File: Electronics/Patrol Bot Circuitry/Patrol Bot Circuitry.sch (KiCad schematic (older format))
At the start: 2 parts

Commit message: A lot
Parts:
- added J?: Conn_01x08, symbol Connector_Generic:Conn_01x08
- added U?: TB6612FNG, Package_SO:SSOP-24_5.3x8.2mm_P0.65mm, symbol Driver_Motor:TB6612FNG
- added U?: MP1584EN, symbol MP1584EN:MP1584EN
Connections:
- net labels added: 3.3V
- wire segments 2 -> 31
- no-connect marks 0 -> 4
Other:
- note added: "ESP-32 Cam\n"
- note added: "Must have pin headers for ESP \nb/c it must be removed when \nuploading since IO0, IO3, and \nIO1 must be used during \nflashing. However, during \nruntime, those pins can be \nused as outputs."
- moved on the sheet: U?

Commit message: Update
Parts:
- removed J?: Conn_01x08, symbol Connector_Generic:Conn_01x08
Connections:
- no-connect marks 4 -> 10
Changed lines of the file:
@@
 $EndComp
-Wire Wire Line
-	4350 5800 4600 5800
-Wire Wire Line
-	4600 5800 4600 4250
-Wire Wire Line
-	4600 4250 4650 4250
-Wire Wire Line
-	4350 5700 4550 5700
-Wire Wire Line
-	4550 5700 4550 4150
-Wire Wire Line
-	4550 4150 4650 4150
-Wire Wire Line
-	4350 5500 4500 5500
-Wire Wire Line
-	4500 5500 4500 4050
-Wire Wire Line
-	4500 4050 4650 4050
-Wire Wire Line
-	4350 5400 4450 5400
-Wire Wire Line
-	4450 5400 4450 3950
-Wire Wire Line
-	4450 3950 4650 3950
 Wire Wire Line
 	4350 5300 4400 5300
@@
 	-1   0    0    1
 $EndComp
-$Comp
-L Connector_Generic:Conn_01x08 J?
-U 1 1 61A3F5ED
-P 2350 3850
-F 0 "J?" H 2430 3842 50  0000 L CNN
-F 1 "Conn_01x08" H 2430 3751 50  0000 L CNN
-F 2 "" H 2350 3850 50  0001 C CNN
-F 3 "~" H 2350 3850 50  0001 C CNN
-	1    2350 3850
-	1    0    0    -1
-$EndComp
+NoConn ~ 3450 6600
+NoConn ~ 3550 6600
+NoConn ~ 3650 6600
+NoConn ~ 3650 4600
+NoConn ~ 3450 4600
+NoConn ~ 5850 3550
+Wire Wire Line
+	4450 5400 4450 3950
+Wire Wire Line
+	4450 3950 4650 3950
+Wire Wire Line
+	4350 5400 4450 5400
+Wire Wire Line
+	4350 5500 4500 5500
+Wire Wire Line
+	4500 5500 4500 4050
+Wire Wire Line
+	4500 4050 4650 4050
+Wire Wire Line
+	4350 5700 4550 5700
+Wire Wire Line
+	4550 5700 4550 4150
+Wire Wire Line
+	4550 4150 4650 4150
+Wire Wire Line
+	4350 5800 4600 5800
+Wire Wire Line
+	4600 5800 4600 4250
+Wire Wire Line
+	4600 4250 4650 4250
 $EndSCHEMATC

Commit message: Update
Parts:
- added D?: D_Photo, symbol Device:D_Photo
- added R?: R, symbol Device:R
- added U?: MCP23017-E_SP, DIP787W45P254L3556H508Q28, symbol MCP23017-E_SP:MCP23017-E_SP
- added U?: MAX9814, symbol MAX9814_:MAX9814
- added U? (x2): HC-SR04, XCVR_HC-SR04, symbol HC-SR04:HC-SR04
- added U?: ADS1115, symbol ADS1115:ADS1115
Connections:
- net 3.3V: now also D?.2 (A)
- net GND: now also R?.2, U?.10 (VSS), U?.15 (A0), U?.16 (A1), U?.17 (A2), U?.2 (GND), U?.4 (GND), U?.4 (GND), U?.5 (ADDR), U?.5 (GND)
- net at U?.4 (OUTPUT-): now also U?.P$2 (GND); no longer U?.P$1 (5V)
- net SDA: now reaches U?.P$10 (IO1/U0T)
- net SDA: now also U?.13 (SDA), U?.4 (SDA)
- net SCL: now reaches U?.P$11 (IO3/U0R)
- net SCL: now also U?.12 (SCL), U?.3 (SCL)
- net 5V: now reaches U?.1 (OUTPUT+)
- net 5V: now also U?.P$1 (5V), U?.1 (VCC), U?.1 (VCC), U?.1 (VDD), U?.4 (VCC), U?.9 (VDD); no longer U?.P$2 (GND)
- new net: U?.1 (GPB0), U?.2 (TRIG)
- new net: U?.2 (GPB1), U?.3 (ECHO)
- new net: U?.2 (TRIG), U?.7 (GPB6)
- new net: U?.3 (ECHO), U?.8 (GPB7)
- new net: D?.1 (K), R?.1, U?.8 (A1)
- new net A0: U?.2 (OUT), U?.7 (A0)
- no-connect marks 10 -> 11
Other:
- note added: "1"
- note added: "11/27/2021\n"
- note added: "Connect ADDR to \nGND for address 0x48,\nVDD for address 0x49,\nSDA for address 0x4A,\nSCL for address 0x4B"
- moved on the sheet: U?

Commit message: Circuit Update
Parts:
- removed U?: TB6612FNG, Package_SO:SSOP-24_5.3x8.2mm_P0.65mm, symbol Driver_Motor:TB6612FNG
- added J?: Conn_01x03_Male, symbol Connector:Conn_01x03_Male
- added J? (x2): Screw_Terminal_01x02, symbol Connector:Screw_Terminal_01x02
- added J?: Left_Motor, symbol Connector:Screw_Terminal_01x02
- added J?: Right_Motor, symbol Connector:Screw_Terminal_01x02
- added Q? (x2): IRF4905, Package_TO_SOT_THT:TO-220-3_Vertical, symbol Transistor_FET:IRF4905
- added Q?: IRLZ44N, Package_TO_SOT_THT:TO-220-3_Vertical, symbol Transistor_FET:IRLZ44N
- added R?: 600K, symbol Device:R
- added R?: 200K, symbol Device:R
- added R?: 2K, symbol Device:R
- added U?: ROB-14450, MODULE_ROB-14450, symbol ROB-14450:ROB-14450
- added VR?: LM317T_NOPB, TO254P1054X470X1955-3, symbol LM317T_NOPB:LM317T_NOPB
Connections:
- net 3.3V: now also U?.4 (VCC)
- net 5V: now also J?.2 (Pin_2), Q?.2 (D), Q?.3 (S), U?.2 (VCC); no longer U?.1 (OUTPUT+), U?.4 (VCC)
- net GND: now also U?.10 (A3), U?.3 (OUTPUT-), U?.4 (OUTPUT-), U?.6 (INPUT-), U?.P$2 (GND), J?.1 (Pin_1), J?.1 (Pin_1), J?.1 (Pin_1), R?.2, U?.3 (GND)
- net SCL: now also U?.23 (SCL), U?.P$15 (IO16); no longer U?.P$11 (IO3/U0R)
- net SDA: now also U?.24 (SDA), U?.P$14 (IO0); no longer U?.P$10 (IO1/U0T)
- net at U?.P$3 (IO12): now also U?.16 (PWMA)
- net at U?.P$4 (IO13): now also U?.15 (AI1)
- net at U?.P$5 (IO15): now also U?.14 (AI2)
- net at U?.P$6 (IO14): now also U?.12 (BI1)
- net at U?.P$7 (IO2): now also U?.11 (BI2)
- net at U?.P$8 (IO4): now also U?.10 (PWMB)
- net 10VOut: now reaches U?.2 (OUTPUT+)
- net 10VOut: now also Q?.3 (S)
- net +10V: now reaches U?.7 (INPUT+)
- net +10V: now also J?.2 (Pin_2), VR?.3 (VIN)
- net at D?.1 (K), R?.1: now also U?.9 (A2); no longer U?.8 (A1)
- net VCC: no longer names the net of U?.8 (INPUT+)
- net VCC: now also Q?.3 (S)
- new net: R?.2, VR?.1 (ADJ)
- new net: J?.1 (Pin_1), U?.4 (A01)
- new net: J?.2 (Pin_2), U?.5 (A02)
- new net: J?.1 (Pin_1), U?.6 (B01)
- new net: J?.2 (Pin_2), U?.7 (B02)
- new net 10V: Q?.1 (G), Q?.1 (G), Q?.1 (G), U?.1 (VM)
- new net A1: R?.1, R?.2, U?.8 (A1)
- new net Battery: J?.2 (Pin_2), Q?.2 (D), R?.1, R?.1, VR?.2 (VOUT)
- new net BatteryOut: Q?.2 (D), U?.1 (OUTPUT+)
- new net IO3: J?.3 (Pin_3), U?.P$11 (IO3/U0R)
- no-connect marks 11 -> 36
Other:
- note added: "ADC for converting sensor readings\nto digital signals for monitoring."
- note added: "Accelerometer and gyroscope sensor."
- note added: "Buck converter that steps down\n10V to 5V for the esp32-cam."
- note added: "Charges the battery when connected\nto electrical outlet. ~~0.67 mA\n"
- note added: "H-Bridge that allows \nsignal amplification for\ncontrolling DC motor."
- note added: "Microphone for picking up sounds\nand detecting danger."
- note added: "Provide addition GPIO pins."
- note added: "Screw terminal for power supplies."
- note added: "See below for reference to ESP32 with servo:\nhttps://randomnerdtutorials.com/esp32-cam-pan-and-tilt-2-axis/"
- note added: "Sonar sensors for providing physical space\ndetection and room memory."
- note added: "Switch circuit that switches to 10V\ninput power supply when it is present \nand charges battery."
- note added: "Voltage divider to monitor battery voltage.\n"
- moved on the sheet: D?, R?, U?

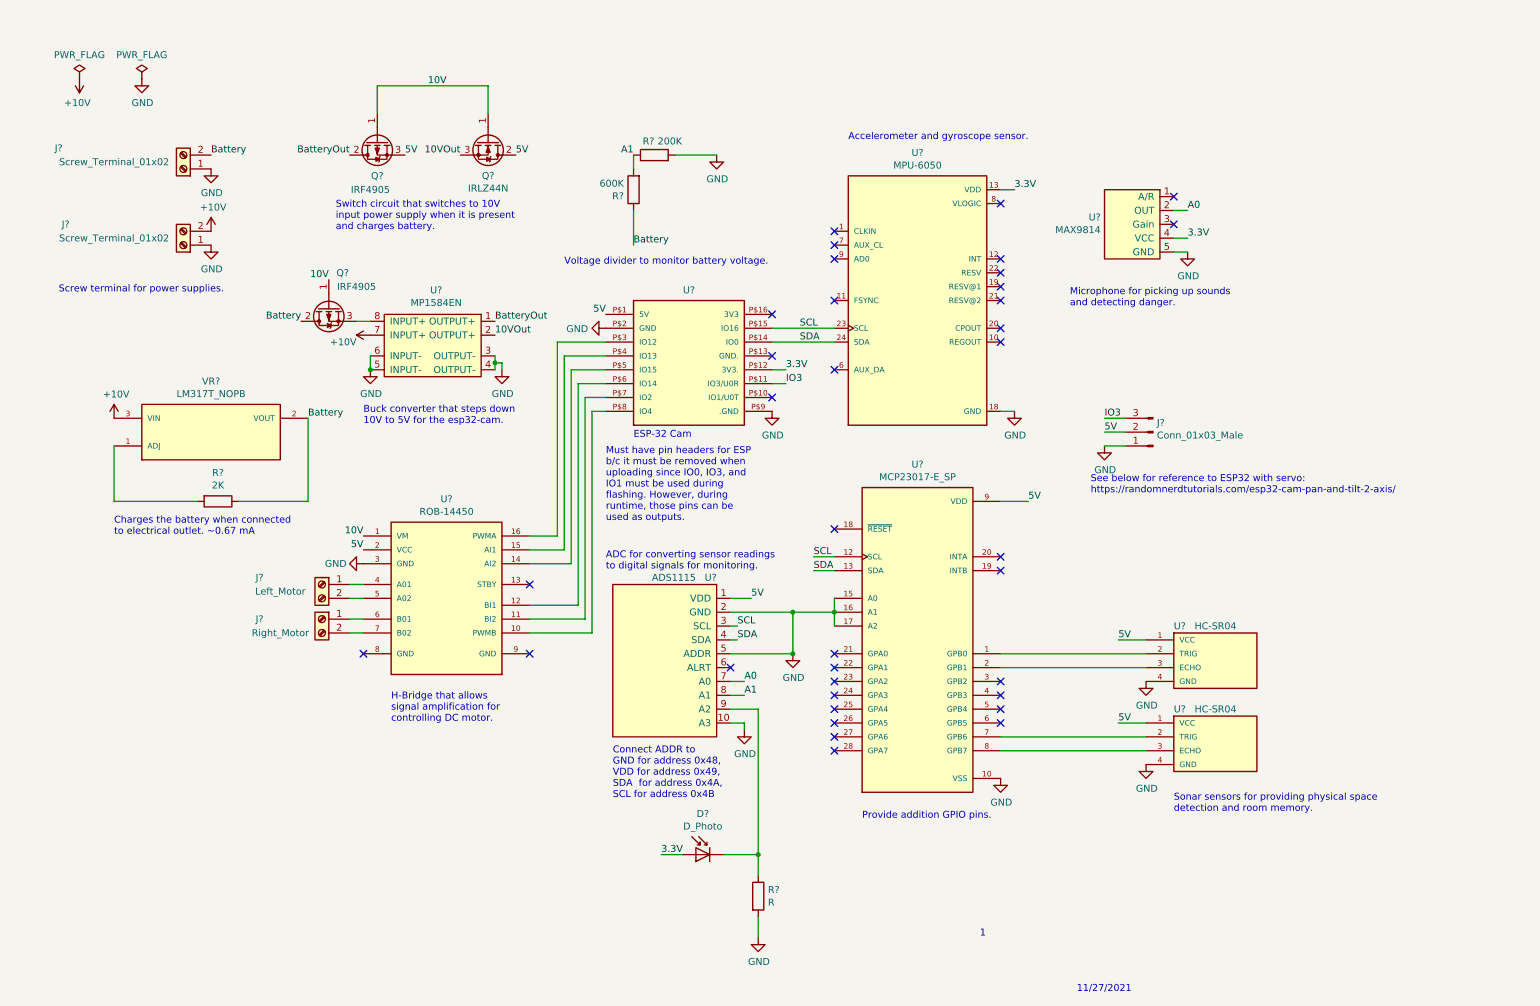
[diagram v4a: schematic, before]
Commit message: Reorganized schematic to aid debugging.
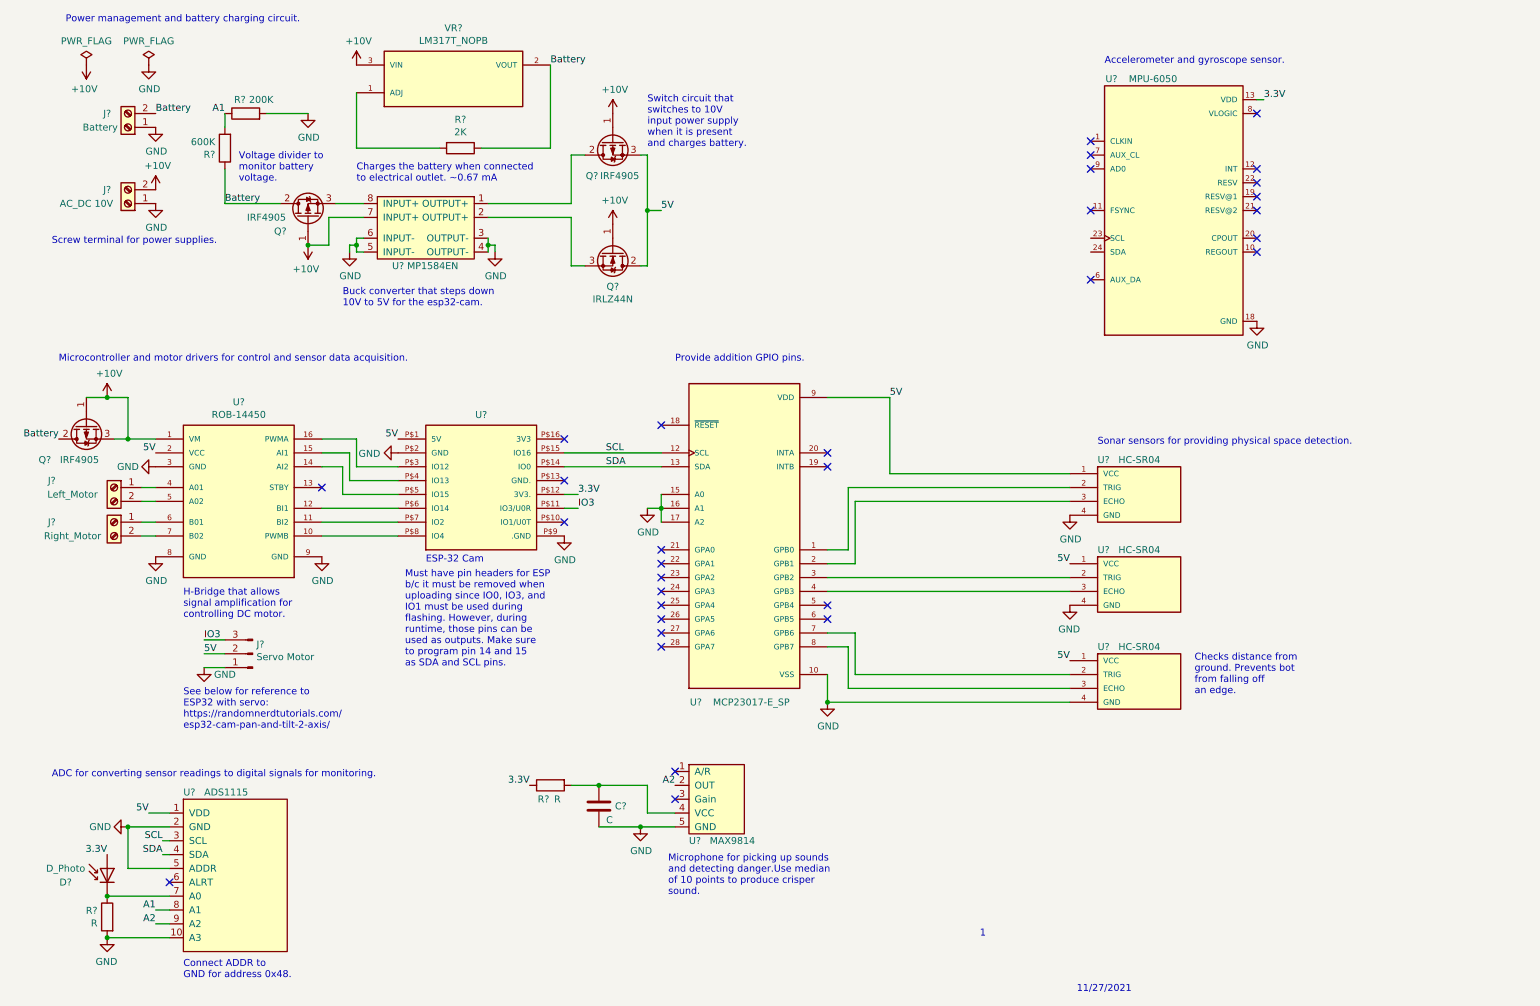
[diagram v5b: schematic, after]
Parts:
- added C?: C, symbol Device:C
- added Q?: IRF4905, Package_TO_SOT_THT:TO-220-3_Vertical, symbol Transistor_FET:IRF4905
- added R?: R, symbol Device:R
- added U?: HC-SR04, XCVR_HC-SR04, symbol HC-SR04:HC-SR04
- J?: value Conn_01x03_Male -> Servo Motor
- J?: value Screw_Terminal_01x02 -> Battery
- J?: value Screw_Terminal_01x02 -> AC_DC 10V
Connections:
- net 10V is gone; now on net +10V: Q?.1 (G), Q?.1 (G), Q?.1 (G), U?.1 (VM)
- net +10V: now also Q?.1 (G), Q?.3 (S)
- net 3.3V: now also R?.1; no longer U?.4 (VCC)
- net 5V: now also U?.1 (VCC)
- net Battery: now also Q?.2 (D)
- net GND: now also U?.8 (GND), U?.9 (GND), C?.2, U?.4 (GND)
- net SCL: no longer U?.23 (SCL)
- net SDA: no longer U?.24 (SDA)
- net at U?.3 (GPB2): now also U?.2 (TRIG)
- net at U?.4 (GPB3): now also U?.3 (ECHO)
- net at D?.1 (K), R?.1: now also U?.7 (A0); no longer U?.9 (A2)
- net 10VOut: no longer names the net of Q?.3 (S), U?.2 (OUTPUT+)
- net A0 renamed A2
- net A2: now also U?.9 (A2); no longer U?.7 (A0)
- net BatteryOut: no longer names the net of Q?.2 (D), U?.1 (OUTPUT+)
- new net: C?.1, R?.2, U?.4 (VCC)
- no-connect marks 36 -> 32
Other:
- note added: "ADC for converting sensor readings to digital signals for monitoring."
- note added: "Checks distance from \nground. Prevents bot \nfrom falling off \nan edge."
- note added: "Connect ADDR to \nGND for address 0x48."
- note added: "Microcontroller and motor drivers for control and sensor data acquisition."
- note added: "Microphone for picking up sounds\nand detecting danger.Use median \nof 10 points to produce crisper \nsound."
- note added: "Must have pin headers for ESP \nb/c it must be removed when \nuploading since IO0, IO3, and \nIO1 must be used during \nflashing. However, during \nruntime, those pins can be \nused as outputs. Make sure\nto program pin 14 and 15\nas SDA and SCL pins."
- note added: "Power management and battery charging circuit."
- note added: "See below for reference to \nESP32 with servo:\nhttps://randomnerdtutorials.com/\nesp32-cam-pan-and-tilt-2-axis/"
- note added: "Sonar sensors for providing physical space detection."
- note added: "Switch circuit that \nswitches to 10V\ninput power supply\nwhen it is present \nand charges battery."
- note added: "Voltage divider to \nmonitor battery \nvoltage.\n"
- note removed: "ADC for converting sensor readings\nto digital signals for monitoring."
- note removed: "Connect ADDR to \nGND for address 0x48,\nVDD for address 0x49,\nSDA for address 0x4A,\nSCL for address 0x4B"
- note removed: "Microphone for picking up sounds\nand detecting danger."
- note removed: "Must have pin headers for ESP \nb/c it must be removed when \nuploading since IO0, IO3, and \nIO1 must be used during \nflashing. However, during \nruntime, those pins can be \nused as outputs."
- note removed: "See below for reference to ESP32 with servo:\nhttps://randomnerdtutorials.com/esp32-cam-pan-and-tilt-2-axis/"
- note removed: "Sonar sensors for providing physical space\ndetection and room memory."
- note removed: "Switch circuit that switches to 10V\ninput power supply when it is present \nand charges battery."
- note removed: "Voltage divider to monitor battery voltage.\n"
- moved on the sheet: D?, J?, Q?, R?, U?, VR?

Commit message: Finished debugging schematic
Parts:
- added C?: 470u, symbol Device:C
- added C?: 0.1u, symbol Device:C
- added C? (x6): 20n, symbol Device:C
- added D? (x2): LED, symbol Device:LED
- added R? (x2): R, symbol Device:R
- added U?: LM2931-3.3_TO220, Package_TO_SOT_THT:TO-220-3_Vertical, symbol Regulator_Linear:LM2931-3.3_TO220
- C?: value C -> 470u
- R?: value R -> 100K
- R?: value R -> 30
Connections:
- net +10V: now also C?.2, C?.2, C?.2
- net 3.3V: no longer R?.1, U?.P$12 (3V3.)
- net 5V: now also R?.1, U?.18 (~RESET), C?.1, C?.1, C?.1; no longer U?.1 (VDD)
- net GND: now also C?.1, C?.1, C?.1, C?.2, C?.2, C?.2, C?.2, C?.2, D?.1 (K), D?.1 (K), U?.2 (GND)
- net SCL: now also U?.23 (SCL)
- net SDA: now also U?.24 (SDA)
- net IO1: now reaches U?.P$10 (IO1/U0T)
- net IO1: now also U?.12 (INT)
- net at U?.5 (GPB4): now also R?.2
- net at U?.6 (GPB5): now also R?.2
- net at C?.1, R?.2: now also U?.1 (VI); no longer U?.4 (VCC)
- net at D?.1 (K), R?.1, U?.7 (A0): now also C?.1
- new net: C?.1, U?.3 (VO), U?.4 (VCC)
- new net: D?.2 (A), R?.1 (x2)
- no-connect marks 32 -> 28
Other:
- note added: "DEBUG LEDs\n"
- note added: "Decouples MCU.\n"
- note added: "Microphone for picking up sounds\nand detecting danger. Use median \nof 10 points to produce crisper \nsound."
- note added: "Must initialize !O1 \npin as interrupt.\n"
- note removed: "Microphone for picking up sounds\nand detecting danger.Use median \nof 10 points to produce crisper \nsound."
- moved on the sheet: C?, D?, J?, R?, U?
